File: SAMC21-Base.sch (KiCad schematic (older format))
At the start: 52 parts, among them J1 Conn_01x04, J2 Conn_01x10, J3 Conn_01x10, J5 Conn_ARM_JTAG_SWD_10, U1 ATSAMC21E18A-AUT, U2 TJA1043T, U3 TPS560430Y, U4 MCP1703A, Y1 8MHz

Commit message: specify ferrite bread
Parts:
- L2: value L_Small -> MPZ1608S221A; symbol Device:L_Small -> Device:Ferrite_Bead_Small
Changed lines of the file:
@@
 $EndComp
 $Comp
-L Device:L_Small L2
+L Device:Ferrite_Bead_Small L2
 U 1 1 609201A5
 P 9300 1000
 F 0 "L2" V 9485 1000 50  0000 C CNN
-F 1 "L_Small" V 9394 1000 50  0000 C CNN
+F 1 "MPZ1608S221A" V 9400 1150 50  0000 C CNN
 F 2 "Inductor_SMD:L_0603_1608Metric" H 9300 1000 50  0001 C CNN
 F 3 "~" H 9300 1000 50  0001 C CNN
@@
 Text Label 8000 1000 0    50   ~ 0
 VDDCORE
-Text Label 8600 1000 0    50   ~ 0
+Text Label 8600 1550 1    50   ~ 0
 VDDANA
 $Comp

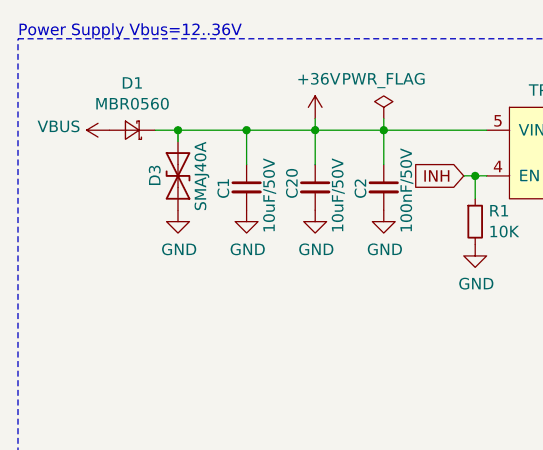
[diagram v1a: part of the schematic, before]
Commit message: place ESD protection before polarity protection
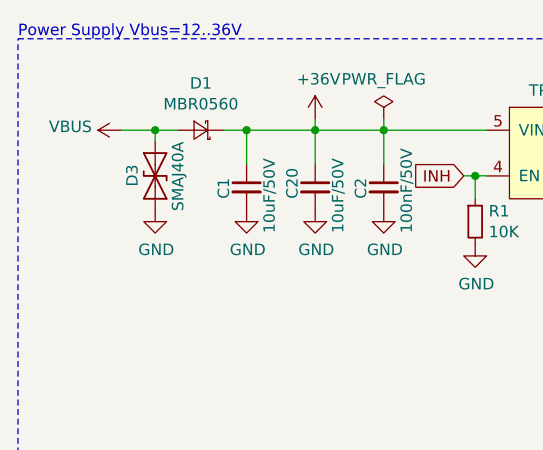
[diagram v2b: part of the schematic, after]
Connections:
- net +36V: no longer D3.1 (A1)
- net VBUS: now also D3.1 (A1)
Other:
- moved on the sheet: D1, D3
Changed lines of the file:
@@
 L Device:D_Schottky_Small D1
 U 1 1 606C00DC
-P 1250 1100
-F 0 "D1" H 1250 895 50  0000 C CNN
-F 1 "MBR0560" H 1250 986 50  0000 C CNN
-F 2 "Diode_SMD:D_SOD-123" V 1250 1100 50  0001 C CNN
-F 3 "~" V 1250 1100 50  0001 C CNN
-	1    1250 1100
+P 1550 1100
+F 0 "D1" H 1550 895 50  0000 C CNN
+F 1 "MBR0560" H 1550 986 50  0000 C CNN
+F 2 "Diode_SMD:D_SOD-123" V 1550 1100 50  0001 C CNN
+F 3 "~" V 1550 1100 50  0001 C CNN
+	1    1550 1100
 	-1   0    0    1
 $EndComp
@@
 L power:VBUS #PWR01
 U 1 1 6080C4AF
-P 1150 1100
-F 0 "#PWR01" H 1150 950 50  0001 C CNN
-F 1 "VBUS" V 1165 1227 50  0000 L CNN
-F 2 "" H 1150 1100 50  0001 C CNN
-F 3 "" H 1150 1100 50  0001 C CNN
-	1    1150 1100
+P 1200 1100
+F 0 "#PWR01" H 1200 950 50  0001 C CNN
+F 1 "VBUS" V 1215 1227 50  0000 L CNN
+F 2 "" H 1200 1100 50  0001 C CNN
+F 3 "" H 1200 1100 50  0001 C CNN
+	1    1200 1100
 	0    -1   -1   0
 $EndComp
@@
 	1    0    0    -1
 $EndComp
-Wire Wire Line
-	1350 1100 1450 1100
 Text GLabel 7600 3200 0    50   Input ~ 0
 RESET
@@
 	1    0    0    -1
 $EndComp
-Connection ~ 1750 1100
 Wire Wire Line
 	2050 1100 2050 1250
@@
 L Device:D_TVS D3
 U 1 1 6139B6D7
-P 1450 1300
-F 0 "D3" H 1400 1200 50  0000 L CNN
-F 1 "SMAJ40A" H 1300 1400 50  0000 L CNN
-F 2 "Diode_SMD:D_SMA" H 1450 1300 50  0001 C CNN
-F 3 "~" H 1450 1300 50  0001 C CNN
-	1    1450 1300
+P 1350 1300
+F 0 "D3" H 1300 1200 50  0000 L CNN
+F 1 "SMAJ40A" H 1200 1400 50  0000 L CNN
+F 2 "Diode_SMD:D_SMA" H 1350 1300 50  0001 C CNN
+F 3 "~" H 1350 1300 50  0001 C CNN
+	1    1350 1300
 	0    1    1    0
 $EndComp
@@
 L power:GND #PWR06
 U 1 1 613A61DE
-P 1450 1450
-F 0 "#PWR06" H 1450 1200 50  0001 C CNN
-F 1 "GND" H 1455 1277 50  0000 C CNN
-F 2 "" H 1450 1450 50  0001 C CNN
-F 3 "" H 1450 1450 50  0001 C CNN
-	1    1450 1450
-	1    0    0    -1
-$EndComp
-Wire Wire Line
-	1450 1150 1450 1100
-Connection ~ 1450 1100
-Wire Wire Line
-	1450 1100 1750 1100
+P 1350 1450
+F 0 "#PWR06" H 1350 1200 50  0001 C CNN
+F 1 "GND" H 1355 1277 50  0000 C CNN
+F 2 "" H 1350 1450 50  0001 C CNN
+F 3 "" H 1350 1450 50  0001 C CNN
+	1    1350 1450
+	1    0    0    -1
+$EndComp
 Text GLabel 9600 2200 2    50   Output ~ 0
 CAN_EN
@@
 NoConn ~ 9600 2500
 NoConn ~ 9600 3000
+Wire Wire Line
+	1750 1100 1650 1100
+Connection ~ 1750 1100
+Wire Wire Line
+	1450 1100 1350 1100
+Wire Wire Line
+	1350 1100 1350 1150
+Wire Wire Line
+	1350 1100 1200 1100
+Connection ~ 1350 1100
 $EndSCHEMATC

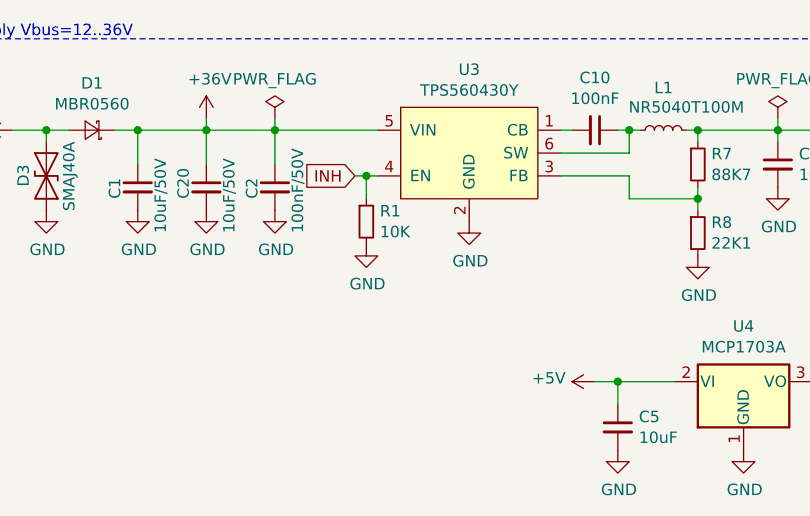
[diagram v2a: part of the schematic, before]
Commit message: burn less energy on INH-pulldown
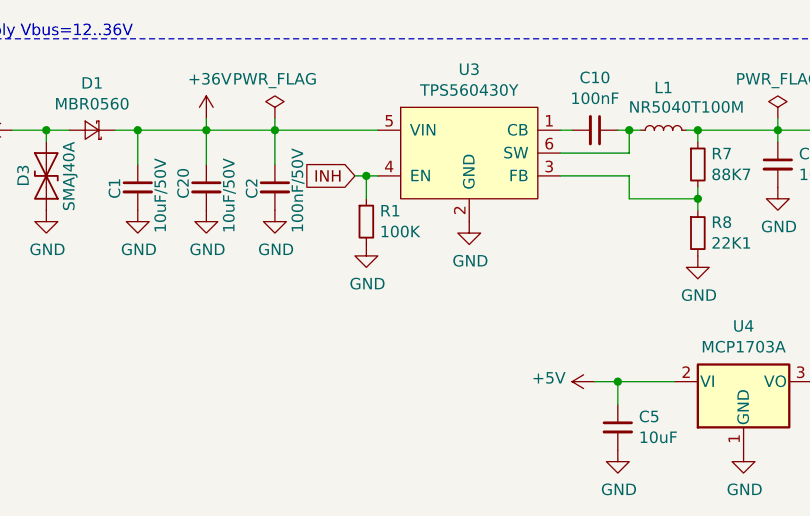
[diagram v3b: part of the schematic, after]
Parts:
- R1: value 10K -> 100K
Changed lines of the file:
@@
 P 2750 1500
 F 0 "R1" H 2809 1546 50  0000 L CNN
-F 1 "10K" H 2809 1455 50  0000 L CNN
+F 1 "100K" H 2809 1455 50  0000 L CNN
 F 2 "Resistor_SMD:R_0603_1608Metric" H 2750 1500 50  0001 C CNN
 F 3 "~" H 2750 1500 50  0001 C CNN

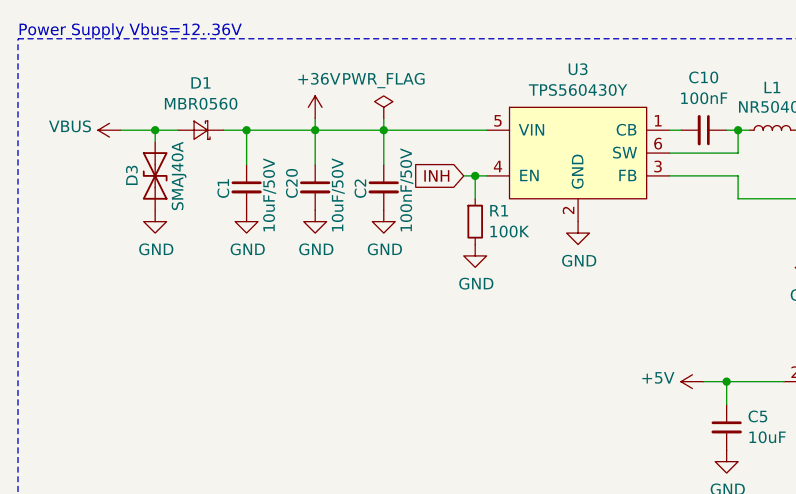
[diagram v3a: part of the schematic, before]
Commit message: change small VIN capacitor rating to 100V
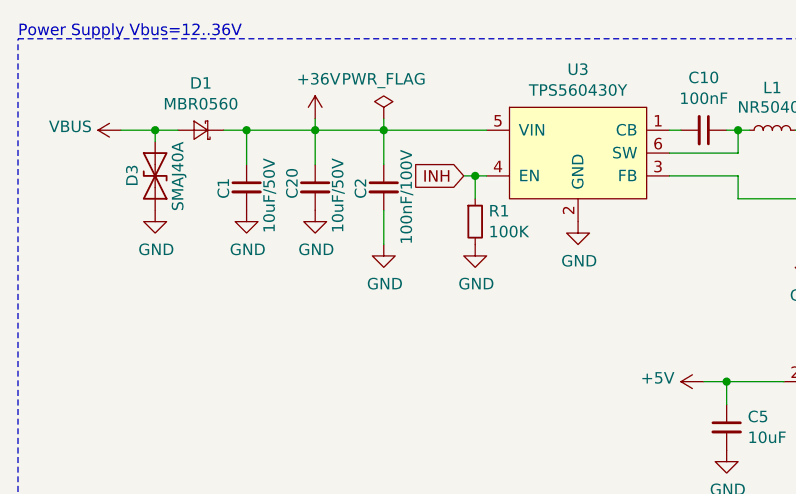
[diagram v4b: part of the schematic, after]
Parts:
- C2: value 100nF/50V -> 100nF/100V
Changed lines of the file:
@@
 Wire Wire Line
 	2050 1100 2350 1100
-Wire Wire Line
-	2350 1100 2350 1250
 Connection ~ 2050 1100
-$Comp
-L power:GND #PWR010
-U 1 1 606C4052
-P 2350 1450
-F 0 "#PWR010" H 2350 1200 50  0001 C CNN
-F 1 "GND" H 2355 1277 50  0000 C CNN
-F 2 "" H 2350 1450 50  0001 C CNN
-F 3 "" H 2350 1450 50  0001 C CNN
-	1    2350 1450
-	1    0    0    -1
-$EndComp
 $Comp
 L power:PWR_FLAG #FLG01
@@
 Text GLabel 4450 6600 2    50   BiDi ~ 0
 CAN_L
-$Comp
-L Device:C_Small C2
-U 1 1 608BF196
-P 2350 1350
-F 0 "C2" V 2250 1300 50  0000 L CNN
-F 1 "100nF/50V" V 2450 1150 50  0000 L CNN
-F 2 "Capacitor_SMD:C_0603_1608Metric" H 2350 1350 50  0001 C CNN
-F 3 "~" H 2350 1350 50  0001 C CNN
-	1    2350 1350
-	1    0    0    -1
-$EndComp
 Text GLabel 7600 3200 0    50   Input ~ 0
 RESET
@@
 	1350 1100 1200 1100
 Connection ~ 1350 1100
+$Comp
+L power:GND #PWR010
+U 1 1 606C4052
+P 2350 1600
+F 0 "#PWR010" H 2350 1350 50  0001 C CNN
+F 1 "GND" H 2355 1427 50  0000 C CNN
+F 2 "" H 2350 1600 50  0001 C CNN
+F 3 "" H 2350 1600 50  0001 C CNN
+	1    2350 1600
+	1    0    0    -1
+$EndComp
+Wire Wire Line
+	2350 1450 2350 1600
+Wire Wire Line
+	2350 1100 2350 1250
+$Comp
+L Device:C_Small C2
+U 1 1 608BF196
+P 2350 1350
+F 0 "C2" V 2250 1300 50  0000 L CNN
+F 1 "100nF/100V" V 2450 1100 50  0000 L CNN
+F 2 "Capacitor_SMD:C_0603_1608Metric" H 2350 1350 50  0001 C CNN
+F 3 "~" H 2350 1350 50  0001 C CNN
+	1    2350 1350
+	1    0    0    -1
+$EndComp
 $EndSCHEMATC

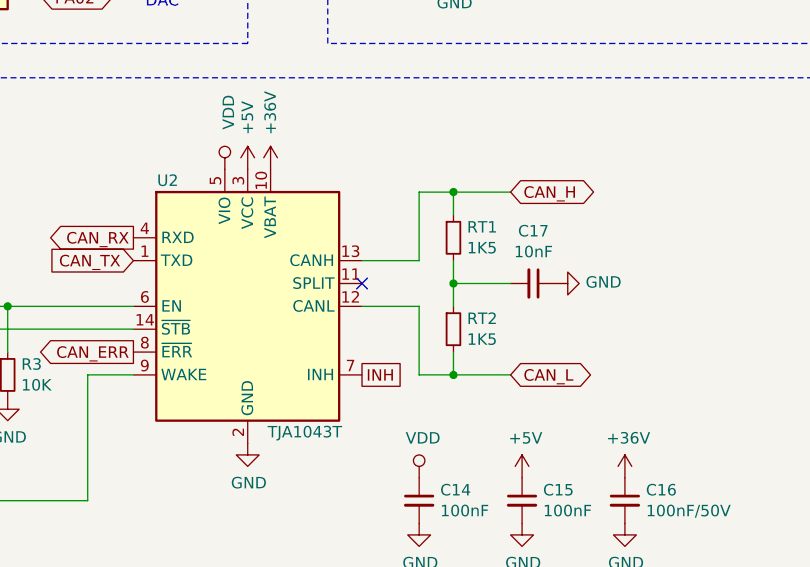
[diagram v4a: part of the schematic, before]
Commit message: connect TJA1043 split pin
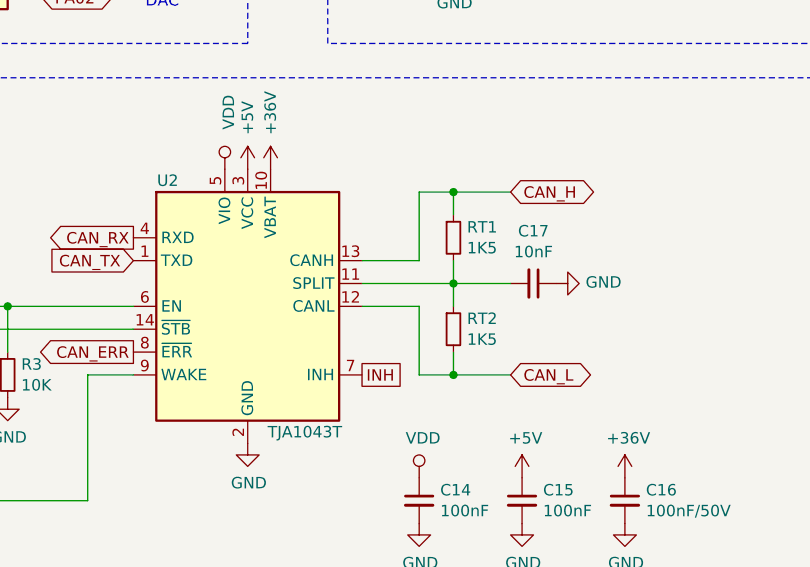
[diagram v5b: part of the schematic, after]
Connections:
- net at U2.11 (SPLIT): now also C17.2, RT1.2, RT2.1
- no-connect marks 8 -> 7
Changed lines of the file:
@@
 Text GLabel 3800 6600 2    50   UnSpc ~ 0
 INH
-NoConn ~ 3800 6200
 $Comp
 L Device:R_Small RT1
@@
 	1    0    0    -1
 $EndComp
+Wire Wire Line
+	3800 6200 4200 6200
 $EndSCHEMATC

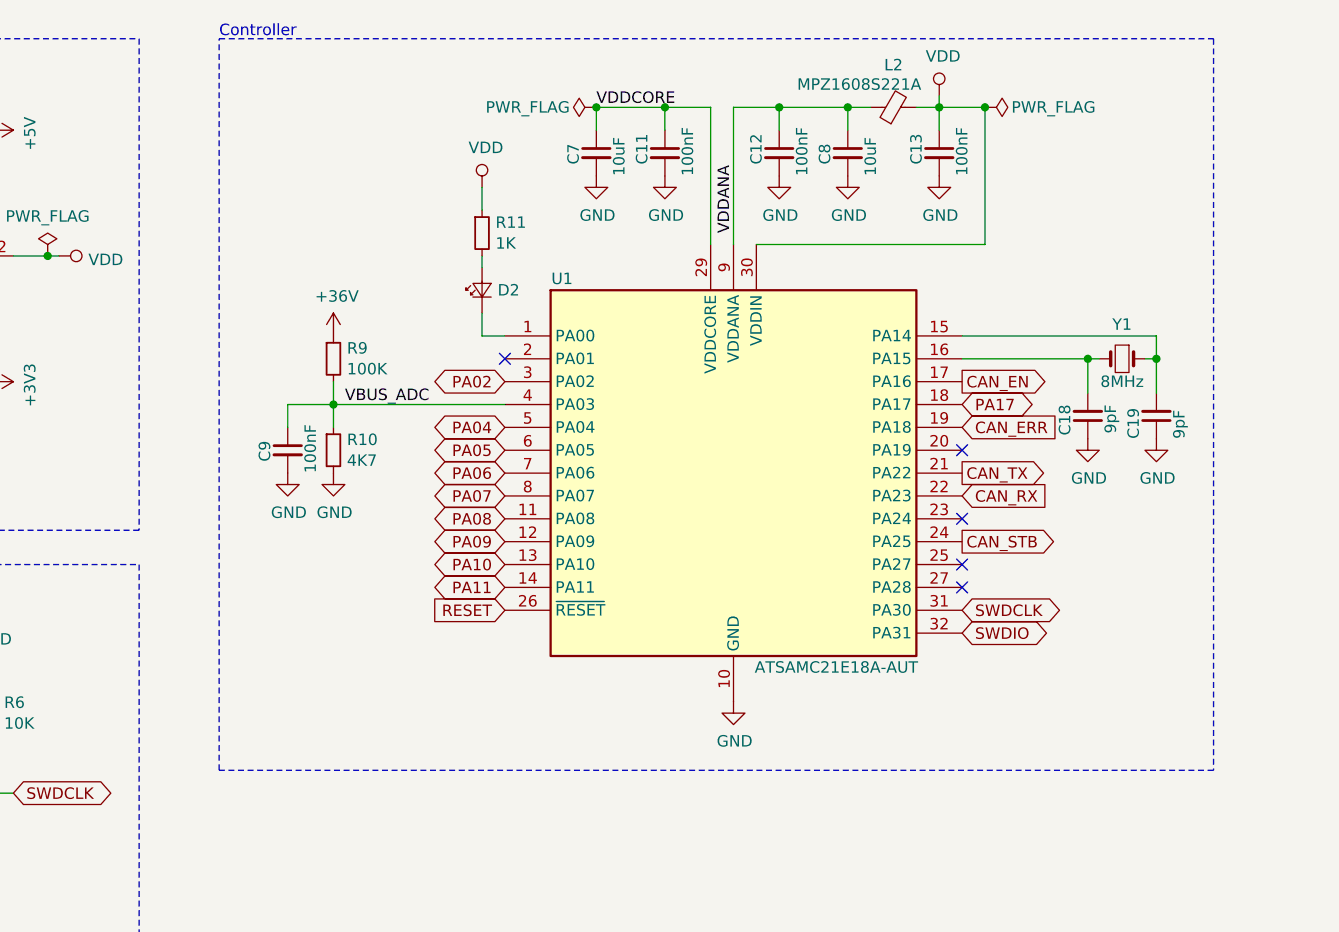
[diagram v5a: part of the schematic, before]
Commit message: specify crystal and crystal Cs
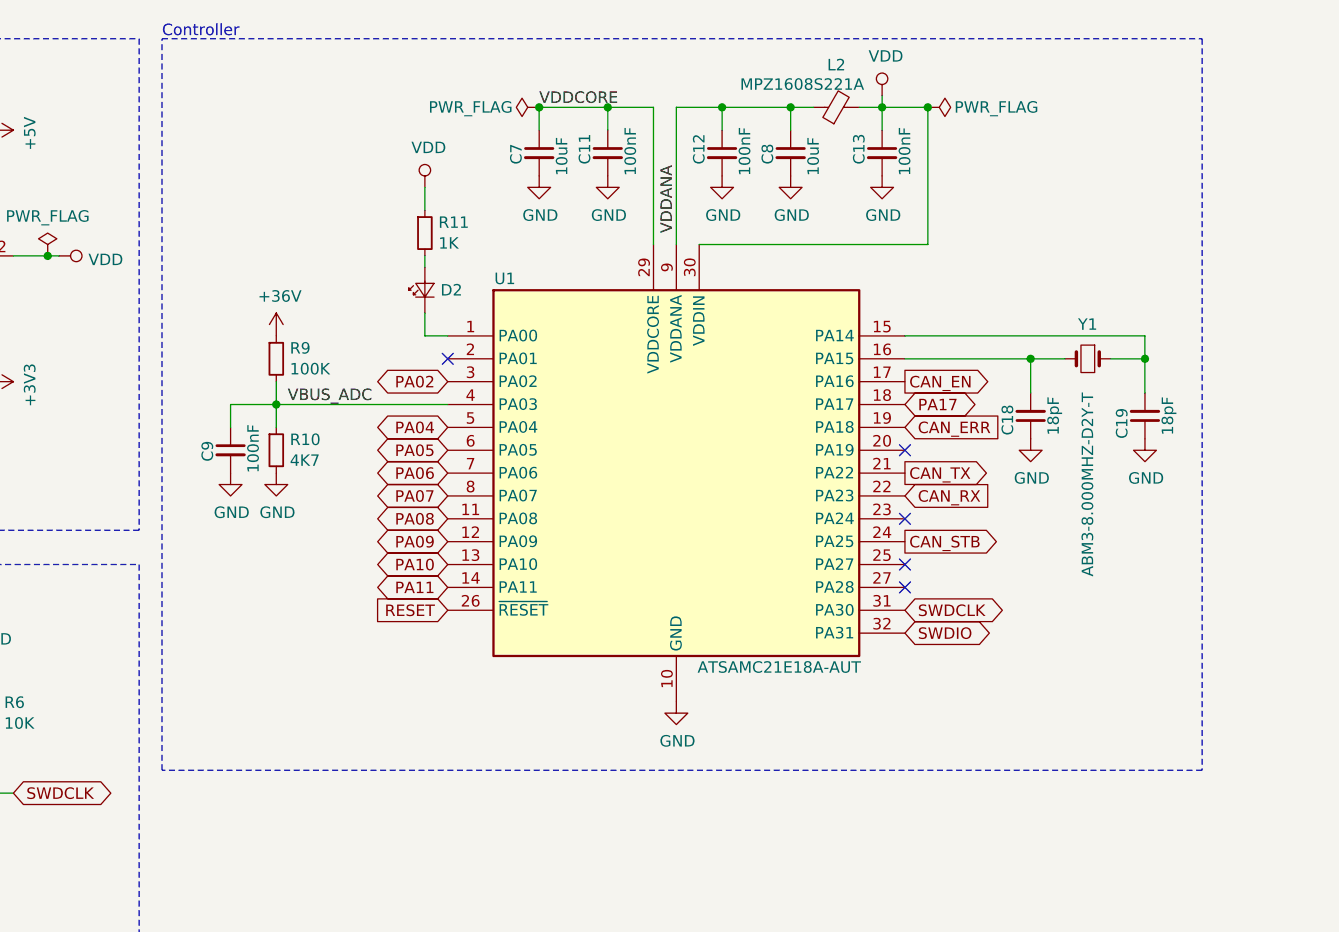
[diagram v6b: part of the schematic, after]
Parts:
- C18, C19: value 9pF -> 18pF
- Y1: value 8MHz -> ABM3-8.000MHZ-D2Y-T
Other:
- moved on the sheet: C11, C12, C13, C18, C19, C7, C8, C9, D2, L2, R10, R11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

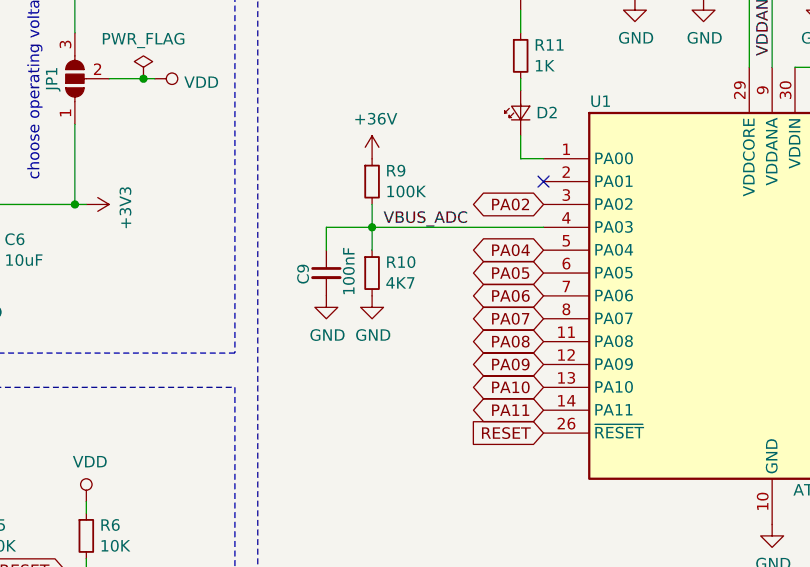
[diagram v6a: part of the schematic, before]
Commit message: change VBUS_ACC volatge divider
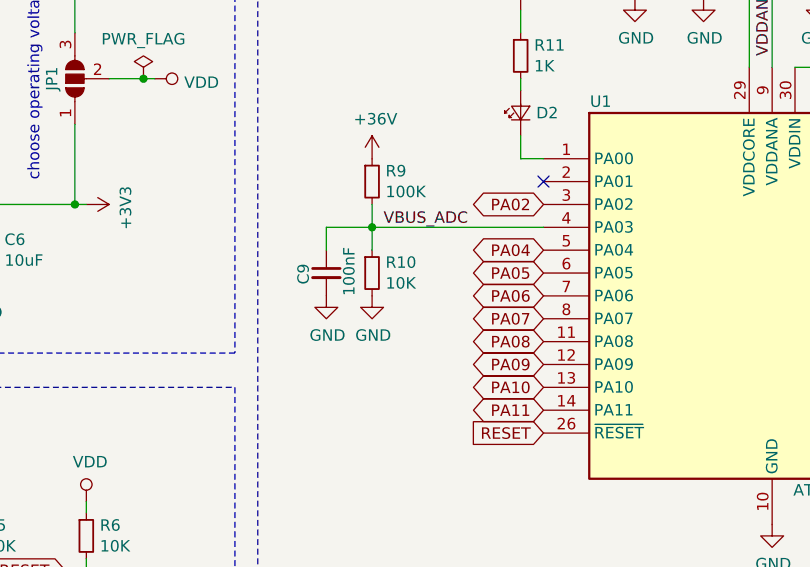
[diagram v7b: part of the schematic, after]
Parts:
- R10: value 4K7 -> 10K
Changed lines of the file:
@@
 P 6600 2500
 F 0 "R10" H 6659 2546 50  0000 L CNN
-F 1 "4K7" H 6659 2455 50  0000 L CNN
+F 1 "10K" H 6659 2455 50  0000 L CNN
 F 2 "Resistor_SMD:R_0603_1608Metric" H 6600 2500 50  0001 C CNN
 F 3 "~" H 6600 2500 50  0001 C CNN
